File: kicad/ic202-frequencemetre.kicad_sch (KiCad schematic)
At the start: 39 parts, among them J1 +12V IN, J2 RF IN, J4 LCD, Q1 2N2369, U1 L7805, U2 LM317L, U3 MB506

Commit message: Correction manuelle de R4 (contre-reaction) + R20 (470k sur pin8 MB506)
R4 corrigee par l'utilisateur directement dans KiCad : elle relie desormais
la base au collecteur de Q1 (contre-reaction continue) au lieu d'etre en
serie entre C10 et la base. Confirmee par lecture du fichier sur disque
avant toute modification.

Ajout de R20 (470k) entre la broche 8 (~IN) du MB506 et GND, placee a cote
de C8 comme demande. C'etait le reseau visible sur le schema relu dont
l'extremite restait ambigue ; il polarise l'entree complementaire vers la
masse pour un pilotage en simple extremite.

Replacement de C8 et R20 en colonne verticale (plutot que cote a cote) pour
eviter le chevauchement de leurs etiquettes de repere/valeur.

ERC : 0 erreur, 0 avertissement. Regles de lisibilite verifiees.

Co-Authored-By: Claude Sonnet 5 <noreply@anthropic.com>
Claude-Session: https://claude.ai/code/session_017jkpXZgM5sH1vt8JFfAijf
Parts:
- added R20: 470K, Resistor_SMD:R_0603_1608Metric, symbol Device:R
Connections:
- net D5_SIG: now also R4.2
- net GND: now also R20.2
- net at C8.1, U3.8 (~{IN}): now also R20.1
- net at C10.2, R4.1: now also Q1.1 (B)
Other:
- moved on the sheet: R4

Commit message: J2 : mini coaxial soude sur 2 pastilles plutot qu'un connecteur SMA
Remplacement de l'empreinte Connector_Coaxial:SMA_Amphenol_132289_EdgeMount
par TestPoint:TestPoint_2Pads_Pitch2.54mm_Drill0.8mm : deux pastilles
traversantes (pas 2,54 mm, percage 0,8 mm) pour souder directement l'ame et
le blindage d'un mini cable coaxial, sans connecteur SMA monte.

Numerotation des pastilles verifiee via pcbnew (1=IN, 2=Ext), coherente
avec le symbole Connector:Conn_Coaxial deja en place ; aucune modification
electrique du schema. ERC : 0 erreur, 0 avertissement.

Co-Authored-By: Claude Sonnet 5 <noreply@anthropic.com>
Claude-Session: https://claude.ai/code/session_017jkpXZgM5sH1vt8JFfAijf
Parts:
- J2: footprint Connector_Coaxial:SMA_Amphenol_132289_EdgeMount -> TestPoint:TestPoint_2Pads_Pitch2.54mm_Drill0.8mm
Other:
- moved on the sheet: C11, C8, R20

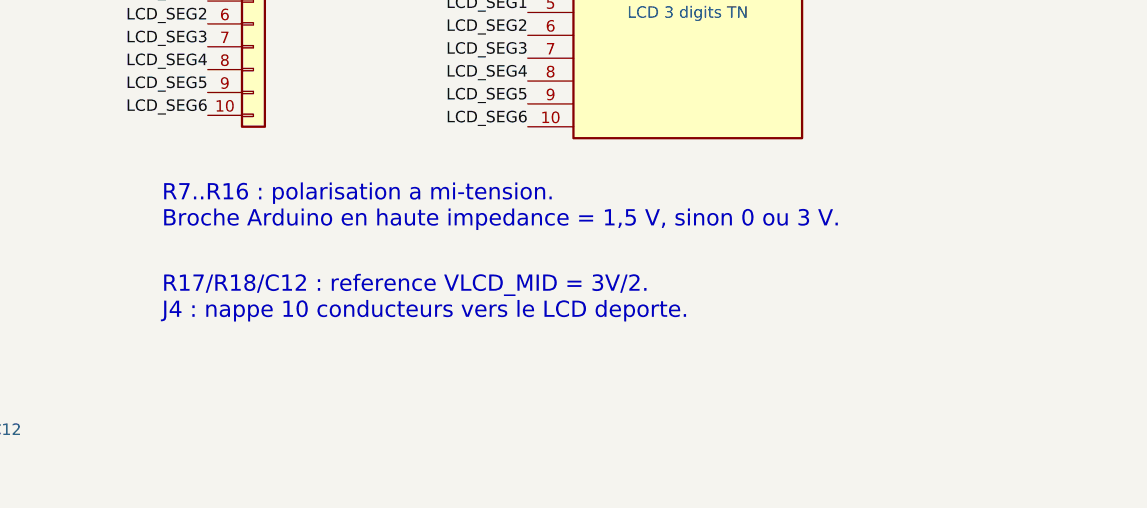
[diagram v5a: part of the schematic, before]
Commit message: J4 : header 2,54mm ; DS1 marque hors carte (monte au bout du cable)
J4 : empreinte remplacee par un header 1x10 P2.54mm vertical
(Connector_PinHeader_2.54mm:PinHeader_1x10_P2.54mm_Vertical), a la place
du connecteur JST-SH 1mm.

DS1 : on_board mis a "no". L'afficheur reste dans le schema et la BOM pour
documenter le systeme complet, mais sync_schematic_to_board ne lui creera
pas d'empreinte sur ce PCB puisqu'il est monte a l'extremite du cable, pas
sur la carte. Note ajoutee sur le schema et dans le README.

ERC : 0 erreur, 0 avertissement. Regles de lisibilite verifiees.

Co-Authored-By: Claude Sonnet 5 <noreply@anthropic.com>
Claude-Session: https://claude.ai/code/session_017jkpXZgM5sH1vt8JFfAijf
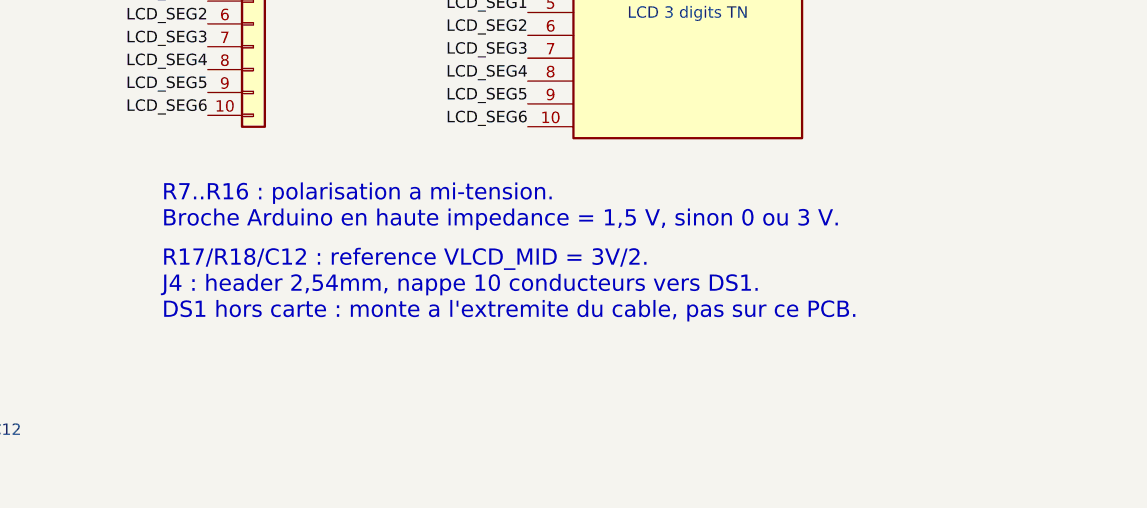
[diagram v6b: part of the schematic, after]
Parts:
- J4: footprint Connector_JST:JST_SH_SM10B-SRSS-TB_1x10-1MP_P1.00mm_Horizontal -> Connector_PinHeader_2.54mm:PinHeader_1x10_P2.54mm_Vertical
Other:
- note added: "R17/R18/C12 : reference VLCD_MID = 3V/2. J4 : header 2,54mm, nappe 10 conducteurs vers DS1. DS1 hors carte : monte a l'extremite du cable, pas sur ce PCB."
- note removed: "R17/R18/C12 : reference VLCD_MID = 3V/2. J4 : nappe 10 conducteurs vers le LCD deporte."
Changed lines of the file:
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@@
 		)
 	)
-	(text "R17/R18/C12 : reference VLCD_MID = 3V/2.\nJ4 : nappe 10 conducteurs vers le LCD deporte."
+	(text "R17/R18/C12 : reference VLCD_MID = 3V/2.\nJ4 : header 2,54mm, nappe 10 conducteurs vers DS1.\nDS1 hors carte : monte a l'extremite du cable, pas sur ce PCB."
 		(exclude_from_sim no)
 		(at 330.2 210.82 0)
@@
 			)
 		)
-		(property "Footprint" "Connector_JST:JST_SH_SM10B-SRSS-TB_1x10-1MP_P1.00mm_Horizontal"
+		(property "Footprint" "Connector_PinHeader_2.54mm:PinHeader_1x10_P2.54mm_Vertical"
 			(at 340.36 175.26 0)
 			(hide yes)
@@
 		(exclude_from_sim no)
 		(in_bom yes)
-		(on_board yes)
+		(on_board no)
 		(in_pos_files yes)
 		(dnp no)

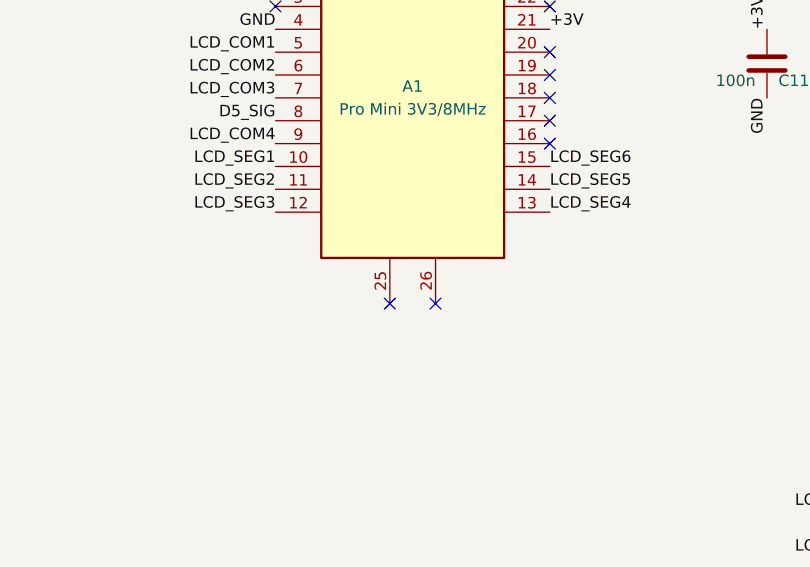
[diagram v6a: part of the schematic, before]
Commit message: Empreinte de A1 : montage sur picots, courtyards des 2 headers uniquement
Le Pro Mini est branche sur deux barrettes de picots femelles, en surelevation
du PCB principal, pour liberer le volume sous le module au profit d'autres
composants. Nouvelle empreinte IC202:Arduino_Pro_Mini_Header_2x12 : 24
broches (2x12, pas 2,54mm, 15,24mm entre rangees), avec un courtyard separe
par rangee - aucun contour de carte complet, aucun courtyard englobant tout
le module, pour ne pas signaler ce volume comme occupe.

Geometrie et ordre physique des broches verifies contre l'empreinte open
source Alarm-Siren/arduino-kicad-library Arduino_Pro_Mini_Socket.kicad_mod
(genuine SparkFun-style Pro Mini) plutot que devines de memoire.

A4/SDA et A5/SCL retirees du symbole IC202:Arduino_Pro_Mini : ce sont des
pastilles au dos du module reel (fil volant necessaire, pas sur les
barrettes), et elles n'etaient deja connectees a rien dans ce projet.
Symbole ramene de 26 a 24 broches, no-connect orphelins supprimes du schema.

Bibliotheque d'empreintes IC202.pretty enregistree en portee projet
(fp-lib-table, chemin ${KIPRJMOD}).

Piege rencontre : un premier essai d'edition directe du .kicad_mod utilisait
des commentaires ";" - syntaxe Lisp absente du format S-expression de KiCad,
qui rendait le fichier illisible par pcbnew (chargement silencieusement
KO) sans erreur de la simple validation sexpdata generique. Corrige.

ERC : 0 erreur, 0 avertissement. Regles de lisibilite verifiees. Chargement
du footprint reconfirme directement via pcbnew apres correction.

Co-Authored-By: Claude Sonnet 5 <noreply@anthropic.com>
Claude-Session: https://claude.ai/code/session_017jkpXZgM5sH1vt8JFfAijf
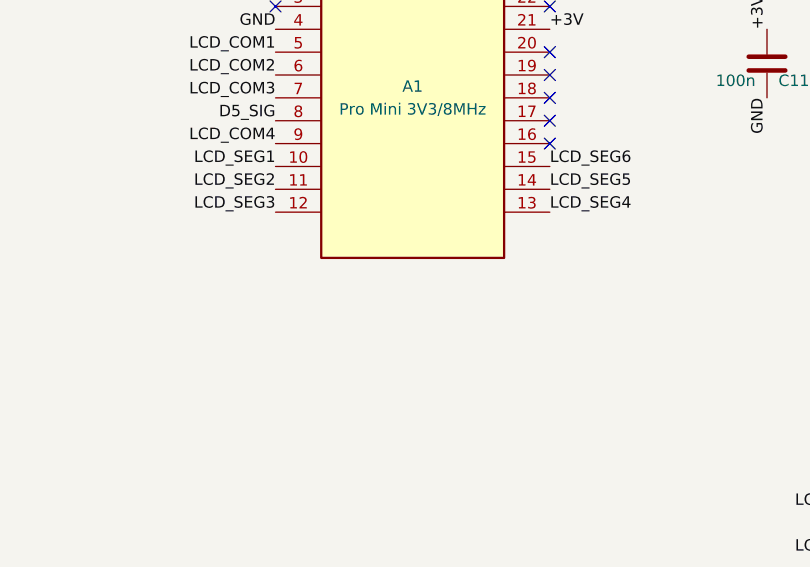
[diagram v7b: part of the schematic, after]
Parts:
- A1: footprint (none) -> IC202:Arduino_Pro_Mini_Header_2x12
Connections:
- no-connect marks 13 -> 11
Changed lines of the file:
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@@
-	)
-	(no_connect
-		(at 238.76 129.54)
 	)
 	(no_connect
@@
 	(no_connect
 		(at 256.54 96.52)
-	)
-	(no_connect
-		(at 243.84 129.54)
 	)
 	(no_connect
@@
 			)
 		)
-		(property "Footprint" ""
+		(property "Footprint" "IC202:Arduino_Pro_Mini_Header_2x12"
 			(at 241.3 101.6 0)
 			(hide yes)
@@
 			)
 		)
-		(property "Description" "Arduino Pro Mini module (ATmega328P), 2x12 pin headers plus A4/A5 inner pins"
+		(property "Description" "Arduino Pro Mini module (ATmega328P), 2x12 pin headers. A4/SDA et A5/SCL (broches arriere, non alignees sur les headers) omises : non utilisees dans ce projet."
 			(at 241.3 96.52 0)
 			(hide yes)

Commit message: Renomme la bibliotheque d'empreintes IC202.pretty -> frequencemetre.pretty
Dossier .pretty et nickname fp-lib-table renommes ensemble (le nickname
suivait le nom du dossier par convention). Reference "Footprint" mise a jour
aux trois endroits : lib_symbols embarque du schema, instance A1, et
bibliotheque de symboles IC202.kicad_sym.

La bibliotheque de symboles (IC202.kicad_sym / sym-lib-table, nickname
IC202) n'est pas concernee, seule la bibliotheque d'empreintes changeait
de nom.

Rechargement pcbnew reconfirme sous le nouveau chemin. ERC : 0 erreur, 0
avertissement.

Co-Authored-By: Claude Sonnet 5 <noreply@anthropic.com>
Claude-Session: https://claude.ai/code/session_017jkpXZgM5sH1vt8JFfAijf
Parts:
- A1: footprint IC202:Arduino_Pro_Mini_Header_2x12 -> frequencemetre:Arduino_Pro_Mini_Header_2x12
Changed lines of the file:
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@@
 			)
 		)
-		(property "Footprint" "IC202:Arduino_Pro_Mini_Header_2x12"
+		(property "Footprint" "frequencemetre:Arduino_Pro_Mini_Header_2x12"
 			(at 241.3 101.6 0)
 			(hide yes)
